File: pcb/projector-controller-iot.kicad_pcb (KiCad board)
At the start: 2 copper layers, 60 x 60 mm, 33 parts, among them J1 DE9_Pins, J2 USB_C_Receptacle, J3 Conn_01x04_Socket, J4 Conn_01x04_Socket, J5 Barrel_Jack, SW1 SW_Push, U1 ESP32-S3-WROOM-1, U2 SP3232EEN-L/TR, U3 LP5907MFX-3.3

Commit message: make fanout make sense
Signed-off-by: 3nt3 <gott@3nt3.de>
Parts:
- moved J3 54.8 mm to (196.5, 76.2), turned to -90 degrees
- moved J5 46.6 mm to (181.0, 111.9), turned to 90 degrees
- moved D4 43.1 mm to (187.4, 104.0), turned to 180 degrees
- moved J1 41.0 mm to (149.0, 89.0), turned to -90 degrees
- moved R7 36.1 mm to (183.9, 104.0), turned to 0 degrees
- moved R4 34.4 mm to (186.2, 62.5), turned to 0 degrees
- moved R5 34.4 mm to (186.2, 64.0), turned to 0 degrees
- moved JP1 33.3 mm to (194.5, 106.5)
- moved J4 30.8 mm to (196.5, 93.2), turned to -90 degrees
- moved J2 28.4 mm to (161.0, 115.5), turned to 0 degrees
- moved D1 27.8 mm to (182.6, 62.5), turned to 180 degrees
- moved D2 27.8 mm to (182.6, 64.0), turned to 180 degrees
- moved C10 27.0 mm to (157.2, 95.6)
- moved C8 26.7 mm to (179.6, 100.4)
- moved C9 26.7 mm to (183.0, 97.5)
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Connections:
- U1 pad 12: Net-(D2-A) -> unconnected-(U1-GPIO8/TOUCH8/ADC1_CH7/SUBSPICS1-Pad12)
- U1 pad 38: unconnected-(U1-GPIO2/TOUCH2/ADC1_CH1-Pad38) -> Net-(D2-A)
- U1 pad 39: unconnected-(U1-GPIO1/TOUCH1/ADC1_CH0-Pad39) -> Net-(D1-A)
- U1 pad 6: Net-(D1-A) -> unconnected-(U1-GPIO6/TOUCH6/ADC1_CH5-Pad6)
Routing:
- net +3V3: track 94.7 -> 142.0 mm, vias 7 -> 2
- net U0TX: track 57.3 -> 23.5 mm, vias 2 -> 0
- net U0RX: track 50.4 -> 24.0 mm, vias 2 -> 0
- net TMS: track 52.1 -> 33.6 mm, vias 2 -> 0
- net USB_D+: track 23.8 -> 41.1 mm
- net TDI: track 50.0 -> 34.3 mm, vias 4 -> 0
- net Net-(JP1-A): track 19.8 -> 35.0 mm
- net USB_D-: track 25.4 -> 40.6 mm
- net U1TX: track 33.1 -> 21.0 mm
- net GND: track 14.9 -> 3.67 mm, vias 56 -> 0
- net TDO: track 46.3 -> 35.6 mm, vias 4 -> 0
- net U1RX: track 29.9 -> 22.1 mm, vias 2 -> 0
- net TCK: track 44.7 -> 37.1 mm, vias 4 -> 0
- net Net-(U1-EN): track 31.8 -> 37.7 mm
- net /RX: track 6.30 -> 11.2 mm
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
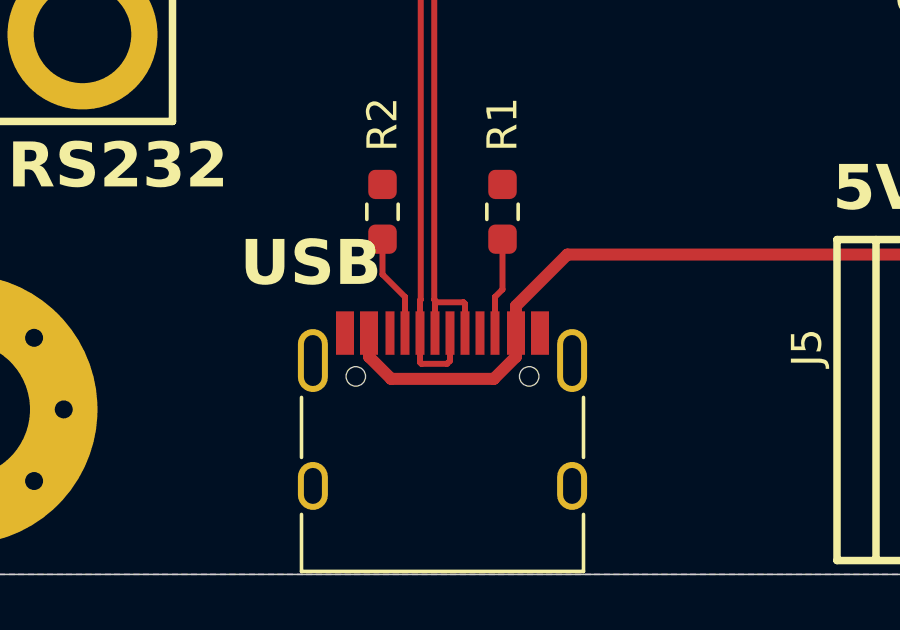
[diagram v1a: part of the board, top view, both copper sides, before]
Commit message: add gitignore
Signed-off-by: 3nt3 <gott@3nt3.de>
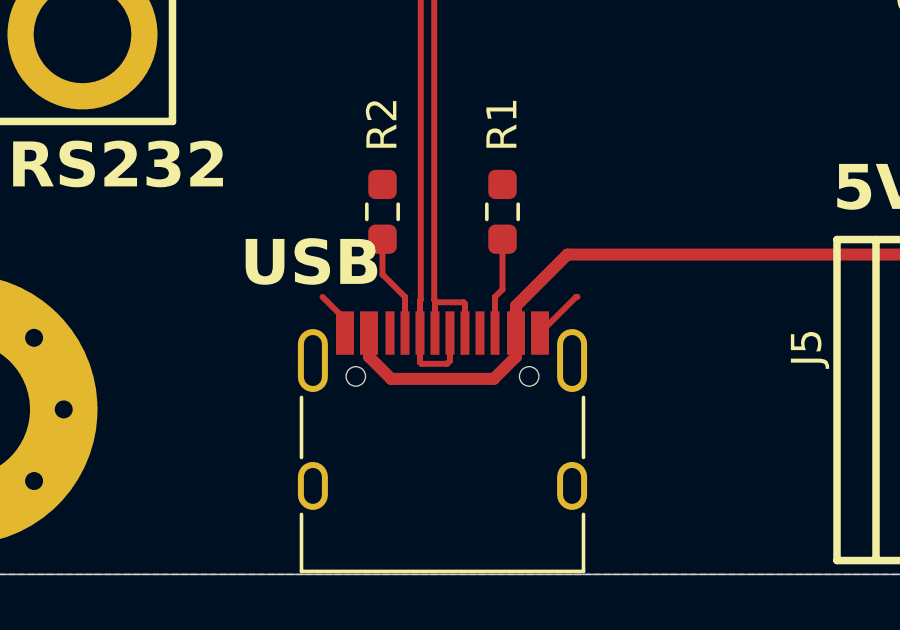
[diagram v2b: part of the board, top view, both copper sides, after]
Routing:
- net GND: track 3.67 -> 6.93 mm

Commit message: Bro idk
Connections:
- U1 pad 13: USB_D+ -> USB_D-
- U1 pad 14: USB_D- -> USB_D+
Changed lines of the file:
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@@
 			(size 1.5 0.9)
 			(layers "F.Cu" "F.Mask" "F.Paste")
-			(net 27 "USB_D+")
+			(net 22 "USB_D-")
 			(pinfunction "GPIO19/U1RTS/ADC2_CH8/CLK_OUT2/USB_D-")
 			(pintype "bidirectional")
@@
 			(size 1.5 0.9)
 			(layers "F.Cu" "F.Mask" "F.Paste")
-			(net 22 "USB_D-")
+			(net 27 "USB_D+")
 			(pinfunction "GPIO20/U1CTS/ADC2_CH9/CLK_OUT1/USB_D+")
 			(pintype "bidirectional")
